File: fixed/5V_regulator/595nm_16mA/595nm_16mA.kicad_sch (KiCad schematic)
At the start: 14 parts, among them J1 Conn_01x04, J2 Conn_01x04, Q1 MMBT5551L, U1 TPS61222DCK, U2 LMV321

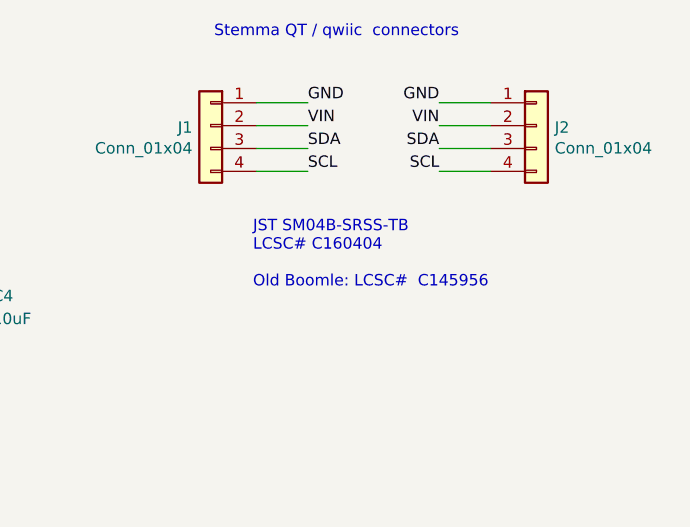
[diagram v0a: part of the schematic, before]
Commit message: Added alternate part for end connector to 595nm design.
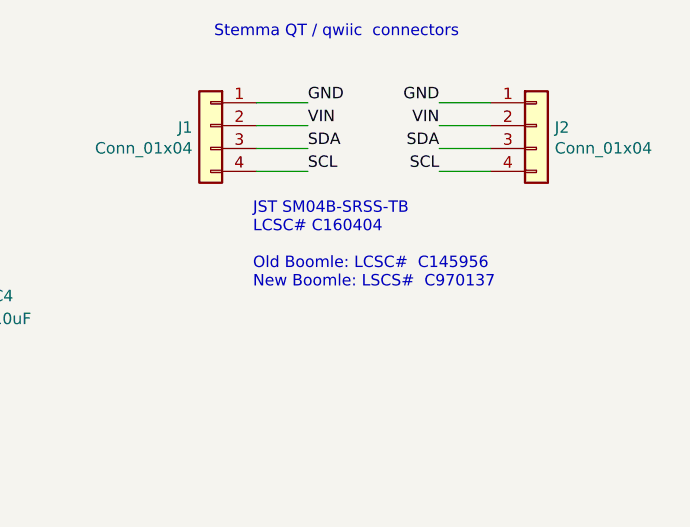
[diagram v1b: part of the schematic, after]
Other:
- note added: "JST SM04B-SRSS-TB LCSC# C160404 Old Boomle: LCSC# C145956 New Boomle: LSCS# C970137"
- note removed: "JST SM04B-SRSS-TB LCSC# C160404 Old Boomle: LCSC# C145956"
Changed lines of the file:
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@@
     (stroke (width 0) (type default))
   )
-  (text "JST SM04B-SRSS-TB\nLCSC# C160404\n\nOld Boomle: LCSC#  C145956\n"
+  (text "JST SM04B-SRSS-TB\nLCSC# C160404\n\nOld Boomle: LCSC#  C145956\nNew Boomle: LSCS#  C970137\n"
     (at 227.457 53.594 0)
     (effects (font (size 1.27 1.27)) (justify left bottom))
@@
     (pin "4")
     (instances
-      (project "white_16mA"
+      (project "595nm_16mA"
         (path "/71f5df2a-3457-4c71-8742-5c7d73c5aae8"
           (reference "J1") (unit 1)
@@
     (pin "4")
     (instances
-      (project "white_16mA"
+      (project "595nm_16mA"
         (path "/71f5df2a-3457-4c71-8742-5c7d73c5aae8"
           (reference "J2") (unit 1)
@@
     (pin "2")
     (instances
-      (project "white_16mA"
+      (project "595nm_16mA"
         (path "/71f5df2a-3457-4c71-8742-5c7d73c5aae8"
           (reference "D1") (unit 1)
@@
     (pin "2")
     (instances
-      (project "white_16mA"
+      (project "595nm_16mA"
         (path "/71f5df2a-3457-4c71-8742-5c7d73c5aae8"
           (reference "R1") (unit 1)
@@
     (pin "1")
     (instances
-      (project "white_16mA"
+      (project "595nm_16mA"
         (path "/71f5df2a-3457-4c71-8742-5c7d73c5aae8"
           (reference "#PWR08") (unit 1)
@@
     (pin "1")
     (instances
-      (project "white_16mA"
+      (project "595nm_16mA"
         (path "/71f5df2a-3457-4c71-8742-5c7d73c5aae8"
           (reference "#FLG0101") (unit 1)
@@
     (pin "1")
     (instances
-      (project "white_16mA"
+      (project "595nm_16mA"
         (path "/71f5df2a-3457-4c71-8742-5c7d73c5aae8"
           (reference "#FLG0102") (unit 1)
@@
     (pin "1")
     (instances
-      (project "white_16mA"
+      (project "595nm_16mA"
         (path "/71f5df2a-3457-4c71-8742-5c7d73c5aae8"
           (reference "#PWR0101") (unit 1)
@@
     (pin "2")
     (instances
-      (project "white_16mA"
+      (project "595nm_16mA"
         (path "/71f5df2a-3457-4c71-8742-5c7d73c5aae8"
           (reference "C4") (unit 1)
@@
     (pin "2")
     (instances
-      (project "white_16mA"
+      (project "595nm_16mA"
         (path "/71f5df2a-3457-4c71-8742-5c7d73c5aae8"
           (reference "C3") (unit 1)
@@
     (pin "1")
     (instances
-      (project "white_16mA"
+      (project "595nm_16mA"
         (path "/71f5df2a-3457-4c71-8742-5c7d73c5aae8"
           (reference "#PWR06") (unit 1)
@@
     (pin "1")
     (instances
-      (project "white_16mA"
+      (project "595nm_16mA"
         (path "/71f5df2a-3457-4c71-8742-5c7d73c5aae8"
           (reference "#PWR011") (unit 1)
@@
     (pin "1")
     (instances
-      (project "white_16mA"
+      (project "595nm_16mA"
         (path "/71f5df2a-3457-4c71-8742-5c7d73c5aae8"
           (reference "#PWR09") (unit 1)
@@
     (pin "1")
     (instances
-      (project "white_16mA"
+      (project "595nm_16mA"
         (path "/71f5df2a-3457-4c71-8742-5c7d73c5aae8"
           (reference "#PWR04") (unit 1)
@@
     (pin "6")
     (instances
-      (project "white_16mA"
+      (project "595nm_16mA"
         (path "/71f5df2a-3457-4c71-8742-5c7d73c5aae8"
           (reference "U1") (unit 1)
@@
     (pin "2")
     (instances
-      (project "white_16mA"
+      (project "595nm_16mA"
         (path "/71f5df2a-3457-4c71-8742-5c7d73c5aae8"
           (reference "C1") (unit 1)
@@
     (pin "1")
     (instances
-      (project "white_16mA"
+      (project "595nm_16mA"
         (path "/71f5df2a-3457-4c71-8742-5c7d73c5aae8"
           (reference "#FLG01") (unit 1)
@@
     (pin "1")
     (instances
-      (project "white_16mA"
+      (project "595nm_16mA"
         (path "/71f5df2a-3457-4c71-8742-5c7d73c5aae8"
           (reference "#PWR05") (unit 1)
@@
     (pin "1")
     (instances
-      (project "white_16mA"
+      (project "595nm_16mA"
         (path "/71f5df2a-3457-4c71-8742-5c7d73c5aae8"
           (reference "#PWR07") (unit 1)
@@
     (pin "2")
     (instances
-      (project "white_16mA"
+      (project "595nm_16mA"
         (path "/71f5df2a-3457-4c71-8742-5c7d73c5aae8"
           (reference "C2") (unit 1)
@@
     (pin "1")
     (instances
-      (project "white_16mA"
+      (project "595nm_16mA"
         (path "/71f5df2a-3457-4c71-8742-5c7d73c5aae8"
           (reference "#PWR010") (unit 1)
@@
     (pin "2")
     (instances
-      (project "white_16mA"
+      (project "595nm_16mA"
         (path "/71f5df2a-3457-4c71-8742-5c7d73c5aae8"
           (reference "R2") (unit 1)
@@
     (pin "4")
     (instances
-      (project "white_16mA"
+      (project "595nm_16mA"
         (path "/71f5df2a-3457-4c71-8742-5c7d73c5aae8"
           (reference "U2") (unit 1)
@@
     (pin "3")
     (instances
-      (project "white_16mA"
+      (project "595nm_16mA"
         (path "/71f5df2a-3457-4c71-8742-5c7d73c5aae8"
           (reference "Q1") (unit 1)
@@
     (pin "2")
     (instances
-      (project "white_16mA"
+      (project "595nm_16mA"
         (path "/71f5df2a-3457-4c71-8742-5c7d73c5aae8"
           (reference "R3") (unit 1)
@@
     (pin "2")
     (instances
-      (project "white_16mA"
+      (project "595nm_16mA"
         (path "/71f5df2a-3457-4c71-8742-5c7d73c5aae8"
           (reference "L1") (unit 1)
